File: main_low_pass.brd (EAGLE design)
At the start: 42.9 x 30.5 mm, 9 parts, among them IC1 74HC14D

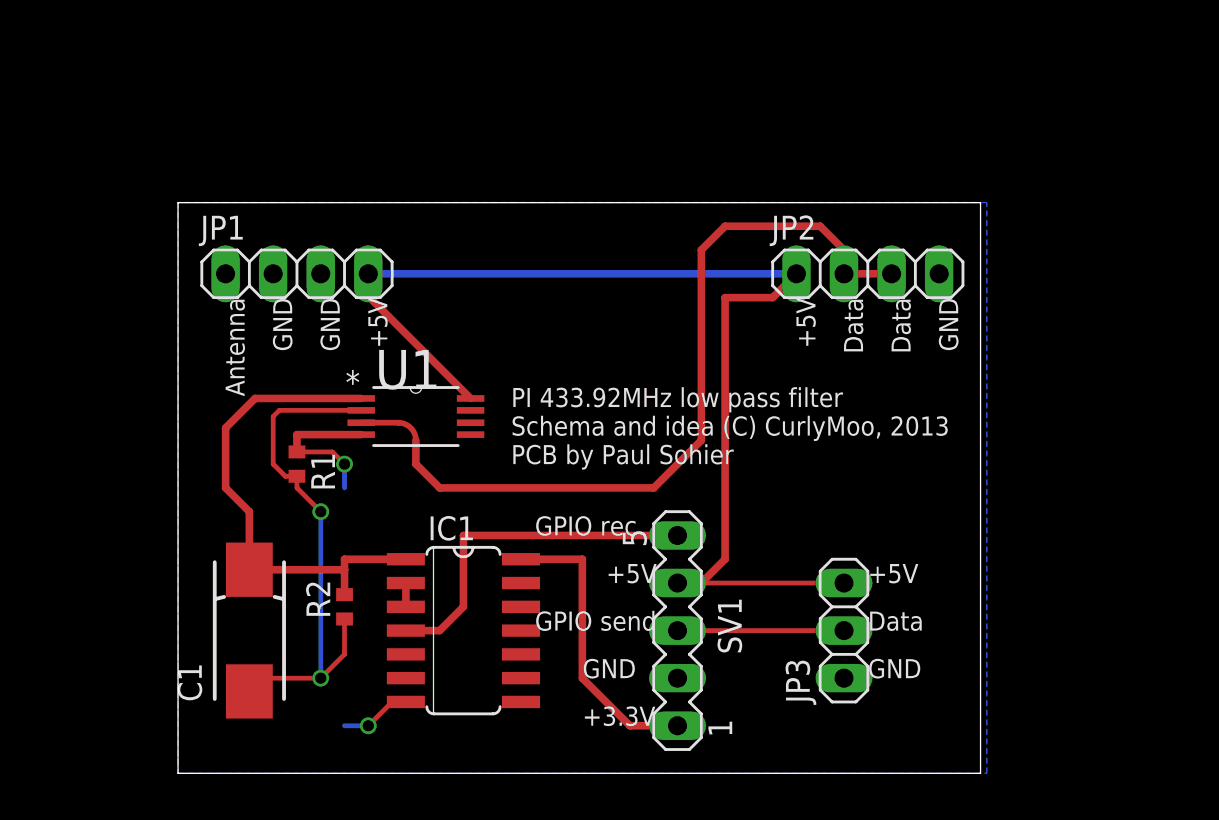
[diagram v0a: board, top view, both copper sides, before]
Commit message: Some updates to the PCB, and a first list of required components.
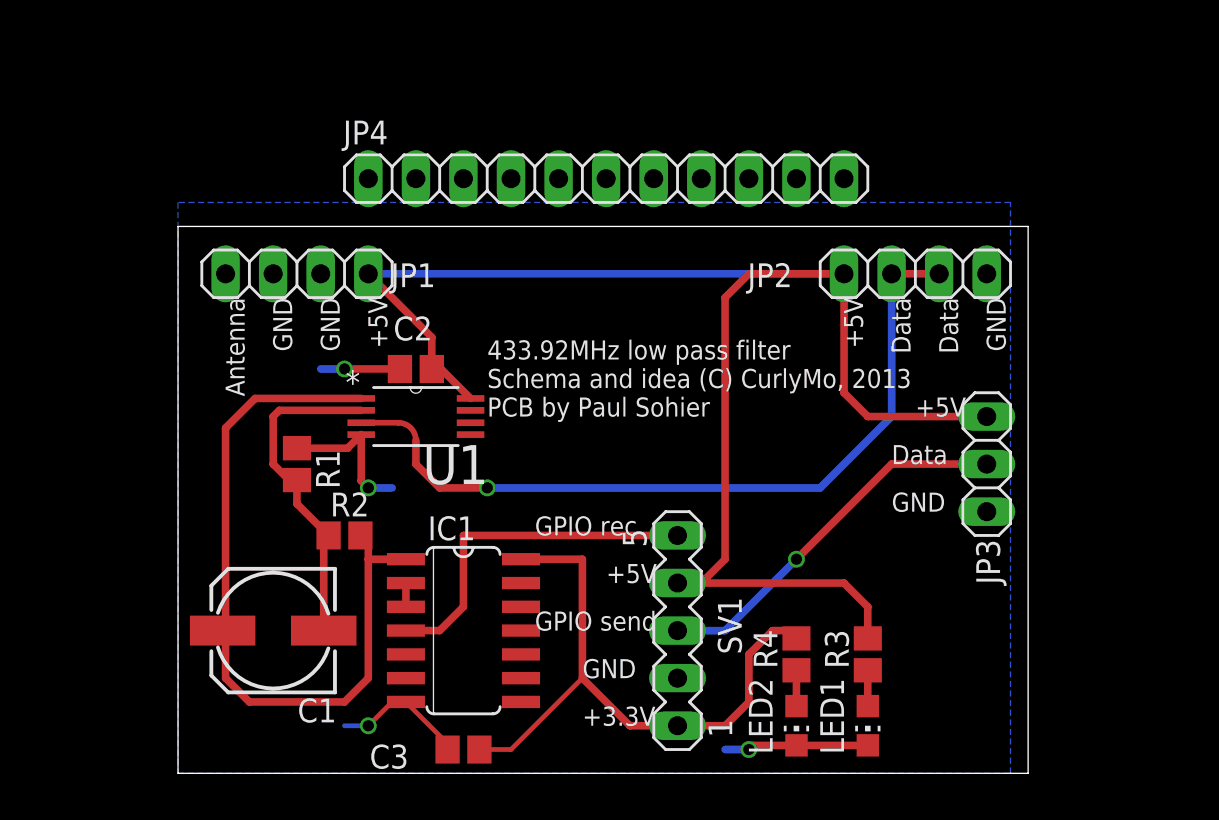
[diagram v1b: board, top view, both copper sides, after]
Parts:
- added C2, C3: (no value), resistor:C0805
- added JP4: (no value), pinhead:1X11
- added LED1, LED2: (no value), led:CHIP-LED0805
- added R3, R4: (no value), resistor:R0805
- C1: device resistor:085CS_1AR -> resistor:153CLV-0605
- IC1: value 74HC14D -> 74HC14N
- R1: device resistor:R1005 -> resistor:R0805
- R2: value 15k -> (none); device resistor:R1005 -> resistor:R0805
- moved JP3 11.7 mm to (43.2, 15.2)
- moved R2 3.81 mm to (8.89, 11.4), turned to 0 degrees
- moved JP2 2.54 mm to (39.4, 25.4)
- moved C1 1.27 mm to (5.08, 6.35), turned to 180 degrees
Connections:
- new net N$8: LED1.A, R3.1
- new net N$9: LED2.A, R4.1
- net GND: now also C2.2, C3.2, LED1.C, LED2.C
- net N$6: now also C2.1, R3.2
- net VCC: now also C3.1, R4.2
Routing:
- net N$6: track 60.8 -> 85.4 mm
- net VCC: track 15.8 -> 33.0 mm
- net GND: track 12.2 -> 27.2 mm, vias 2 -> 4
- net N$7: track 26.9 -> 40.3 mm
- net N$5: track 8.89 -> 20.2 mm, vias 0 -> 1
- net N$2: track 28.0 -> 17.8 mm, vias 2 -> 0
- net N$9: track 0.00 -> 1.91 mm
- net N$8: track 0.00 -> 1.91 mm
- net N$1: track 44.0 -> 42.2 mm, vias 0 -> 1
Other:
- board size 42.9 x 30.5 mm -> 45.4 x 29.2 mm
- board text added: "433.92MHz low pass filter Schema and idea (C) CurlyMo, 2013 PCB by Paul Sohier"
- board text removed: "PI 433.92MHz low pass filter Schema and idea (C) CurlyMoo, 2013 PCB by Paul Sohier"

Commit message: SV1 verplaatst naar de zijkant ipv in het midden van het bord.
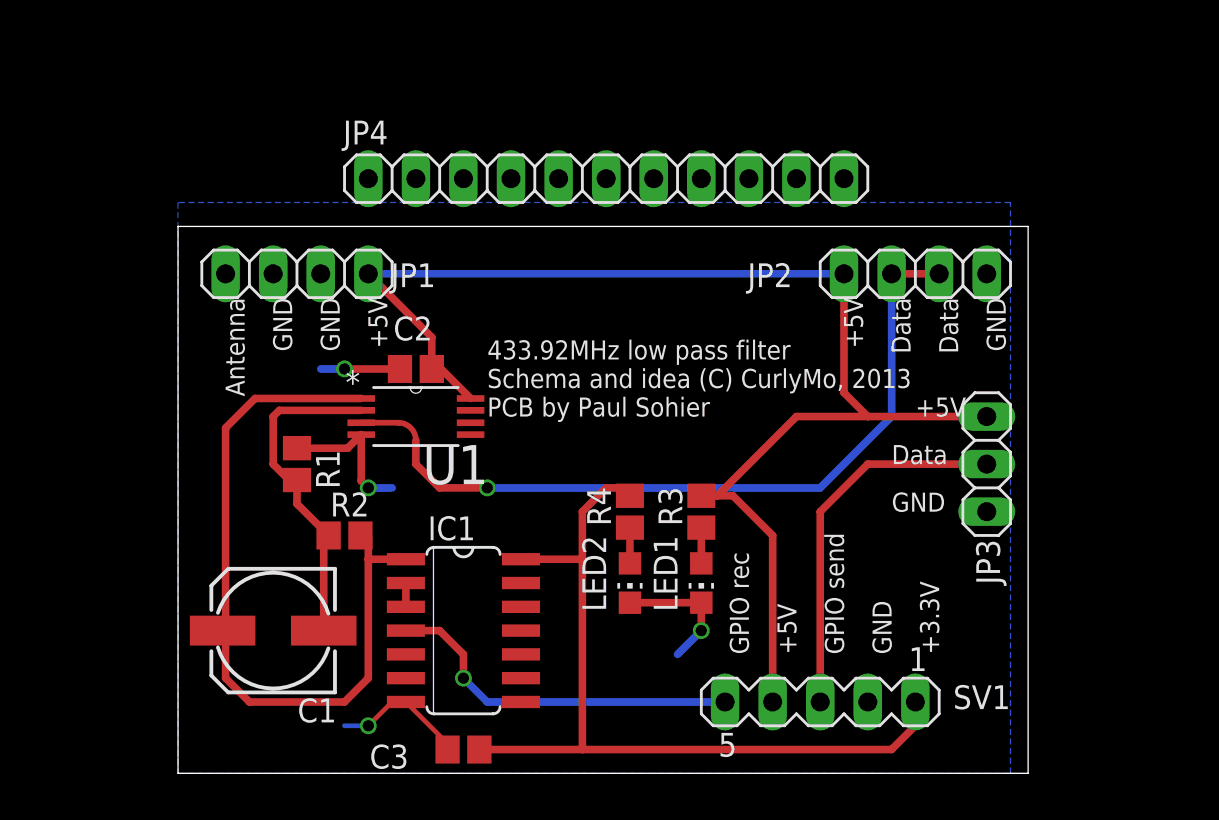
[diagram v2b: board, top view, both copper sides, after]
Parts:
- moved LED2 11.7 mm to (24.1, 8.89)
- moved R4 11.7 mm to (24.1, 12.7)
- moved LED1 11.7 mm to (27.9, 8.89)
- moved R3 11.7 mm to (27.9, 12.7)
- moved SV1 8.52 mm to (34.3, 2.54), turned to 180 degrees
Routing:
- net VCC: track 33.0 -> 46.0 mm
- net N$6: track 85.4 -> 72.5 mm
- net GND: track 27.2 -> 26.6 mm
- net N$4: track 18.8 -> 19.4 mm, vias 0 -> 1
- net N$5: track 20.2 -> 20.1 mm, vias 1 -> 0

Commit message: replace input connector with a headerstrip so it can be clicked on a PI, and added a second strip that copies the input from the pie.
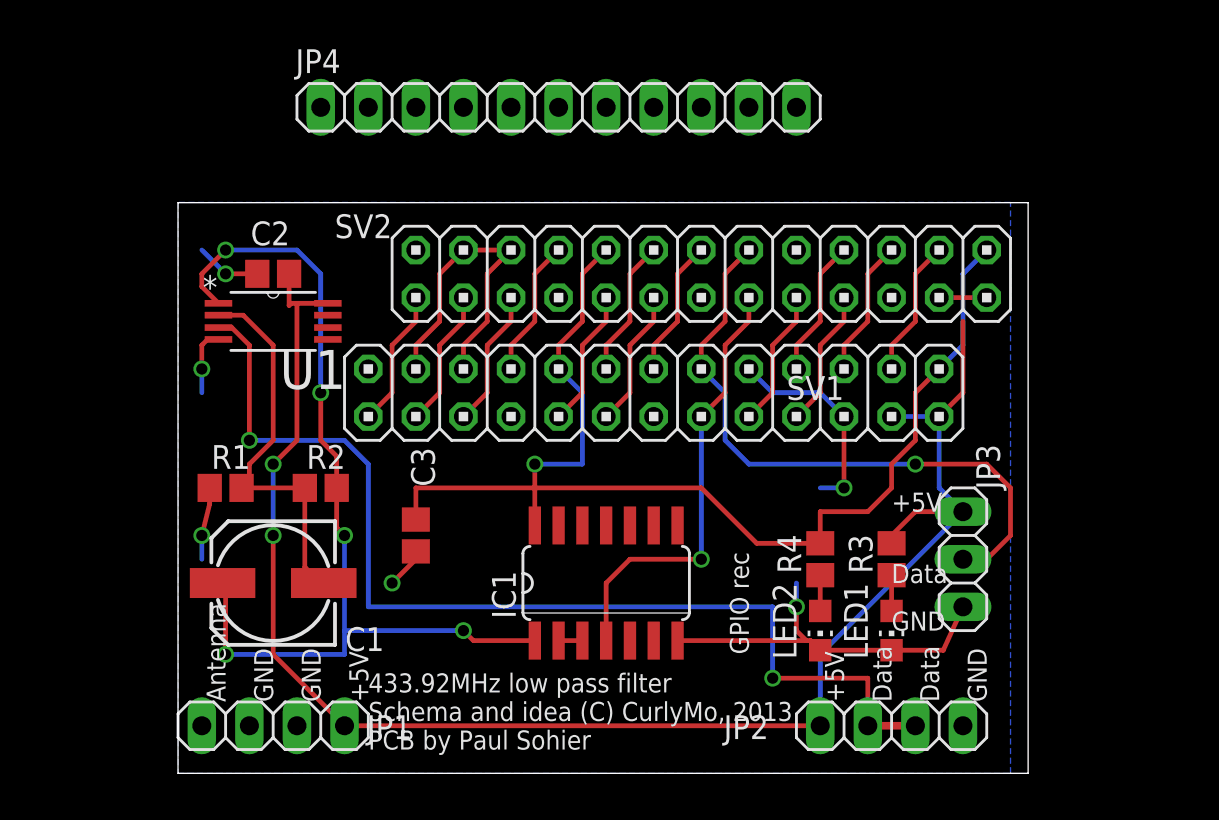
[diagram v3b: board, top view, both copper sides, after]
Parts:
- added SV2: (no value), pinhead:2X13
- IC1: value 74HC14N -> 74HC14D
- SV1: device con-lstb:MA05-1 -> pinhead:2X13
- moved JP1 24.2 mm to (5.08, 1.27)
- moved JP2 24.2 mm to (38.1, 1.27)
- moved SV1 18.8 mm to (25.4, 19.1)
- moved C3 11.7 mm to (12.7, 11.4), turned to 270 degrees
- moved LED1 10.5 mm to (38.1, 6.35)
- moved LED2 10.5 mm to (34.3, 6.35)
- moved R3 10.5 mm to (38.1, 10.2)
- moved R4 10.5 mm to (34.3, 10.2)
- moved C2 9.16 mm to (5.08, 25.4)
- moved U1 9.16 mm to (5.08, 22.9)
- moved IC1 8.03 mm to (22.9, 8.89), turned to 0 degrees
- moved JP3 5.24 mm to (41.9, 10.2)
- moved JP4 4.58 mm to (20.3, 34.3)
- moved R1 4.02 mm to (2.54, 14.0), turned to 0 degrees
- moved R2 2.84 mm to (7.62, 14.0)
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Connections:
- new net N$10: IC1.4, SV1.12, SV2.12
- new net N$11: SV1.10, SV2.10
- new net N$12: SV1.16, SV2.16
- new net N$13: SV1.18, SV2.18
- new net N$14: SV1.22, SV2.22
- new net N$15: SV1.7, SV2.7
- new net N$16: SV1.24, SV2.24
- new net N$17: SV1.26, SV2.26
- new net N$18: SV1.3, SV2.3
- new net N$19: SV1.5, SV2.5
- new net N$21: SV1.13, SV2.13
- new net N$22: SV1.15, SV2.15
- new net N$23: SV1.19, SV2.19
- new net N$24: SV1.21, SV1.23, SV2.21, SV2.23
- net GND: now also SV1.14, SV1.20, SV1.25, SV1.6, SV1.9, SV2.14, SV2.20, SV2.25, SV2.6, SV2.9; no longer SV1.2
- net N$4: now also SV1.8, SV2.8; no longer IC1.4, SV1.5
- net N$5: now also SV1.11, SV2.11; no longer SV1.3
- net N$6: now also SV1.2, SV2.2, SV2.4
- net VCC: now also SV1.17, SV2.1, SV2.17
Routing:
- net N$10: track 0.00 -> 23.7 mm, vias 0 -> 1
- net VCC: track 46.0 -> 64.8 mm, vias 0 -> 1
- net GND: track 26.6 -> 44.6 mm, vias 4 -> 6
- net N$24: track 0.00 -> 17.3 mm
- net N$6: track 72.5 -> 89.5 mm, vias 0 -> 2
- net N$1: track 42.2 -> 57.2 mm, vias 1 -> 2
- net N$5: track 20.1 -> 33.6 mm, vias 0 -> 1
- net N$4: track 19.4 -> 7.40 mm, vias 1 -> 0
- net N$7: track 40.3 -> 50.8 mm, vias 0 -> 5
- net N$21: track 0.00 -> 7.40 mm
- net N$19: track 0.00 -> 7.40 mm
- net N$18: track 0.00 -> 7.40 mm
- net N$15: track 0.00 -> 7.40 mm
- net N$23: track 0.00 -> 7.40 mm
- net N$22: track 0.00 -> 7.40 mm
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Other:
- board size 45.4 x 29.2 mm -> 45.4 x 30.5 mm
- board text removed: "+3.3V"
- board text removed: "GPIO send"

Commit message: Moved some stuff, tried adding a RJ1 connector as test.
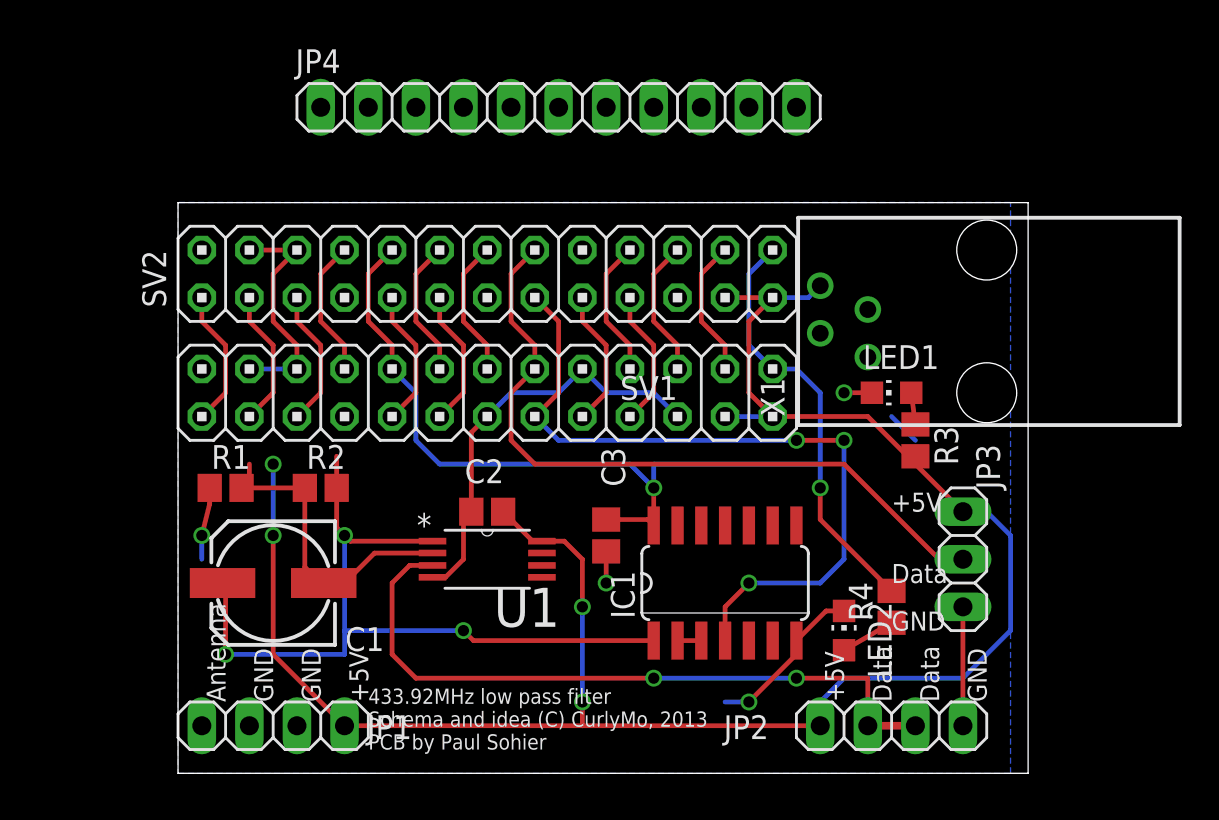
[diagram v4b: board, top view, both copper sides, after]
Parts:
- added X1: 14867, con-4ucon:14867
- moved C2 17.1 mm to (16.5, 12.7)
- moved U1 17.1 mm to (16.5, 10.2)
- moved LED1 12.7 mm to (38.1, 19.1), turned to 90 degrees
- moved SV2 11.4 mm to (16.5, 25.4)
- moved C3 10.2 mm to (22.9, 11.4)
- moved SV1 8.89 mm to (16.5, 19.1)
- moved R3 6.48 mm to (39.4, 16.5), turned to 270 degrees
- moved IC1 6.35 mm to (29.2, 8.89)
- moved R4 4.58 mm to (38.1, 7.62)
- moved LED2 1.27 mm to (35.6, 6.35), turned to 0 degrees
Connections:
- net GND: now also X1.3
- net N$6: now also X1.4
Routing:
- net N$1: track 57.2 -> 37.4 mm
- net N$10: track 23.7 -> 40.0 mm, vias 1 -> 3
- net N$6: track 89.5 -> 104.1 mm, vias 2 -> 4
- net N$7: track 50.8 -> 42.5 mm, vias 5 -> 3
- net N$2: track 20.7 -> 15.6 mm
- net N$24: track 17.3 -> 12.5 mm
- net N$5: track 33.6 -> 38.5 mm, vias 1 -> 0
- net GND: track 44.6 -> 46.4 mm, vias 6 -> 4
- net VCC: track 64.8 -> 63.0 mm, vias 1 -> 2
- net N$9: track 1.91 -> 2.93 mm
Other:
- board text removed: "GPIO rec"

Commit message: Nieuwste revisie, connector omgedraaid zodat hij op de PI kan, RJ11 toegevoegd voor slimme meter.
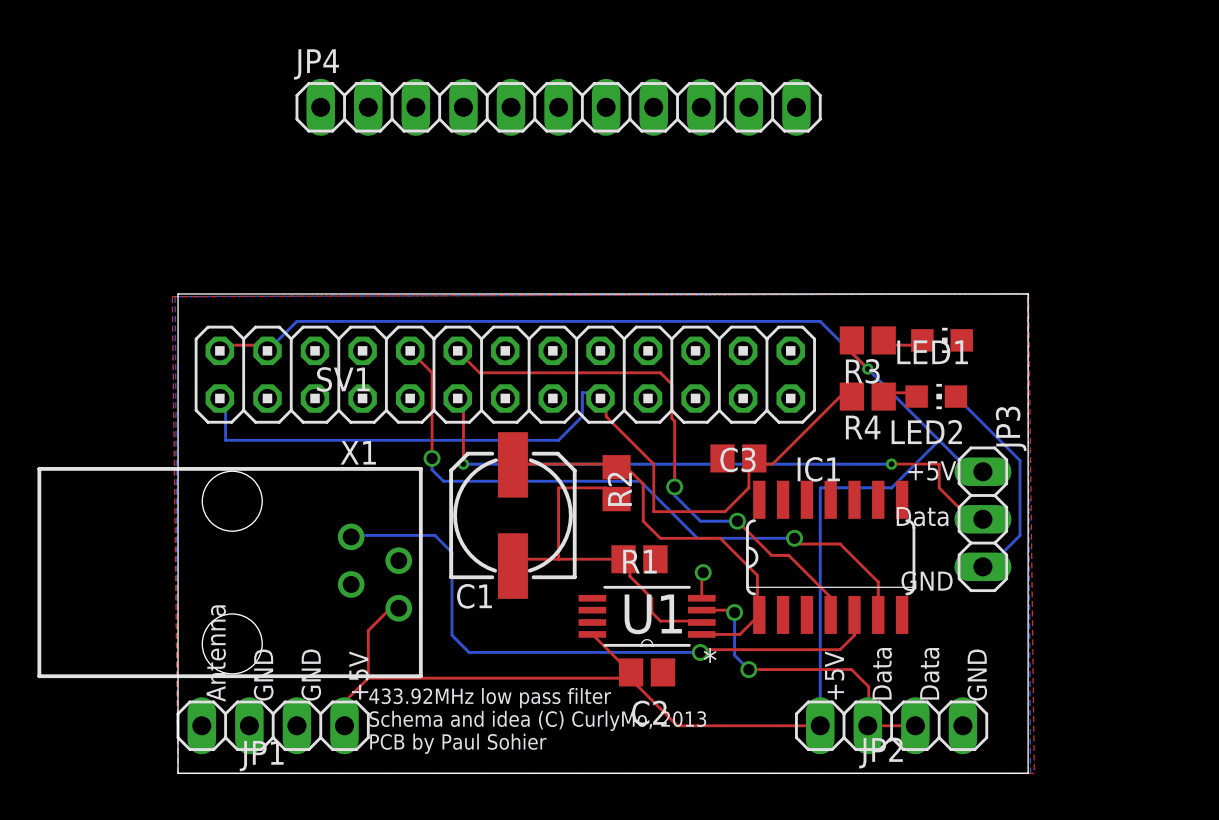
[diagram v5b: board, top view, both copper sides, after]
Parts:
- removed SV2: (no value), pinhead:2X13
- moved X1 42.5 mm to (2.90, 9.45), turned to 270 degrees
- moved R1 22.4 mm to (24.6, 10.2), turned to 180 degrees
- moved R2 15.8 mm to (23.4, 14.2), turned to 90 degrees
- moved LED2 13.4 mm to (40.5, 18.8), turned to 270 degrees
- moved C1 13.3 mm to (17.9, 12.5), turned to 90 degrees
- moved C2 12.1 mm to (25.0, 4.11), turned to 0 degrees
- moved R4 11.3 mm to (36.8, 18.8), turned to 180 degrees
- moved U1 9.06 mm to (25.0, 7.11), turned to 180 degrees
- moved C3 8.17 mm to (29.9, 15.5), turned to 180 degrees
- moved R3 5.91 mm to (36.8, 21.8), turned to 180 degrees
- moved IC1 5.80 mm to (34.8, 10.3)
- moved LED1 3.88 mm to (40.8, 21.8), turned to 270 degrees
- moved JP3 2.39 mm to (43.0, 12.3)
- moved SV1 1.36 mm to (17.5, 20.0), turned to 0 degrees
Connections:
- removed net N$12: SV1.16, SV2.16
- removed net N$13: SV1.18, SV2.18
- removed net N$14: SV1.22, SV2.22
- removed net N$15: SV1.7, SV2.7
- removed net N$16: SV1.24, SV2.24
- removed net N$17: SV1.26, SV2.26
- removed net N$18: SV1.3, SV2.3
- removed net N$19: SV1.5, SV2.5
- removed net N$21: SV1.13, SV2.13
- removed net N$22: SV1.15, SV2.15
- removed net N$23: SV1.19, SV2.19
- removed net N$24: SV1.21, SV1.23, SV2.21, SV2.23
- net GND: no longer SV2.14, SV2.20, SV2.25, SV2.6, SV2.9
- net N$10: no longer SV2.12
- net N$11: now also IC1.6; no longer SV2.10
- net N$4: now also IC1.5, X1.1; no longer SV1.8, SV2.8
- net N$5: no longer SV2.11
- net N$6: no longer SV2.2, SV2.4
- net VCC: now also IC1.11, IC1.13, IC1.9; no longer SV2.1, SV2.17
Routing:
- net GND: track 46.4 -> 13.3 mm, vias 4 -> 1
- net N$11: track 7.40 -> 34.9 mm, vias 0 -> 2
- net N$4: track 7.40 -> 33.6 mm, vias 0 -> 1
- net N$1: track 37.4 -> 16.6 mm
- net N$7: track 42.5 -> 22.5 mm, vias 3 -> 0
- net VCC: track 63.0 -> 47.8 mm, vias 2 -> 0
- net N$24: track 12.5 -> 0.00 mm
- net N$10: track 40.0 -> 29.7 mm, vias 3 -> 2
- net N$19: track 7.40 -> 0.00 mm
- net N$22: track 7.40 -> 0.00 mm
- net N$21: track 7.40 -> 0.00 mm
- net N$23: track 7.40 -> 0.00 mm
- net N$18: track 7.40 -> 0.00 mm
- net N$15: track 7.40 -> 0.00 mm
- net N$17: track 7.40 -> 0.00 mm
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- added copper zone on layer 1, net GND
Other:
- board size 45.4 x 30.5 mm -> 45.4 x 25.6 mm
